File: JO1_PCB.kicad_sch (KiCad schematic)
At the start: 6 parts, among them J1 CN7, J2 CN8, J3 CN9, J4 CN10, U2 module_mpu6050

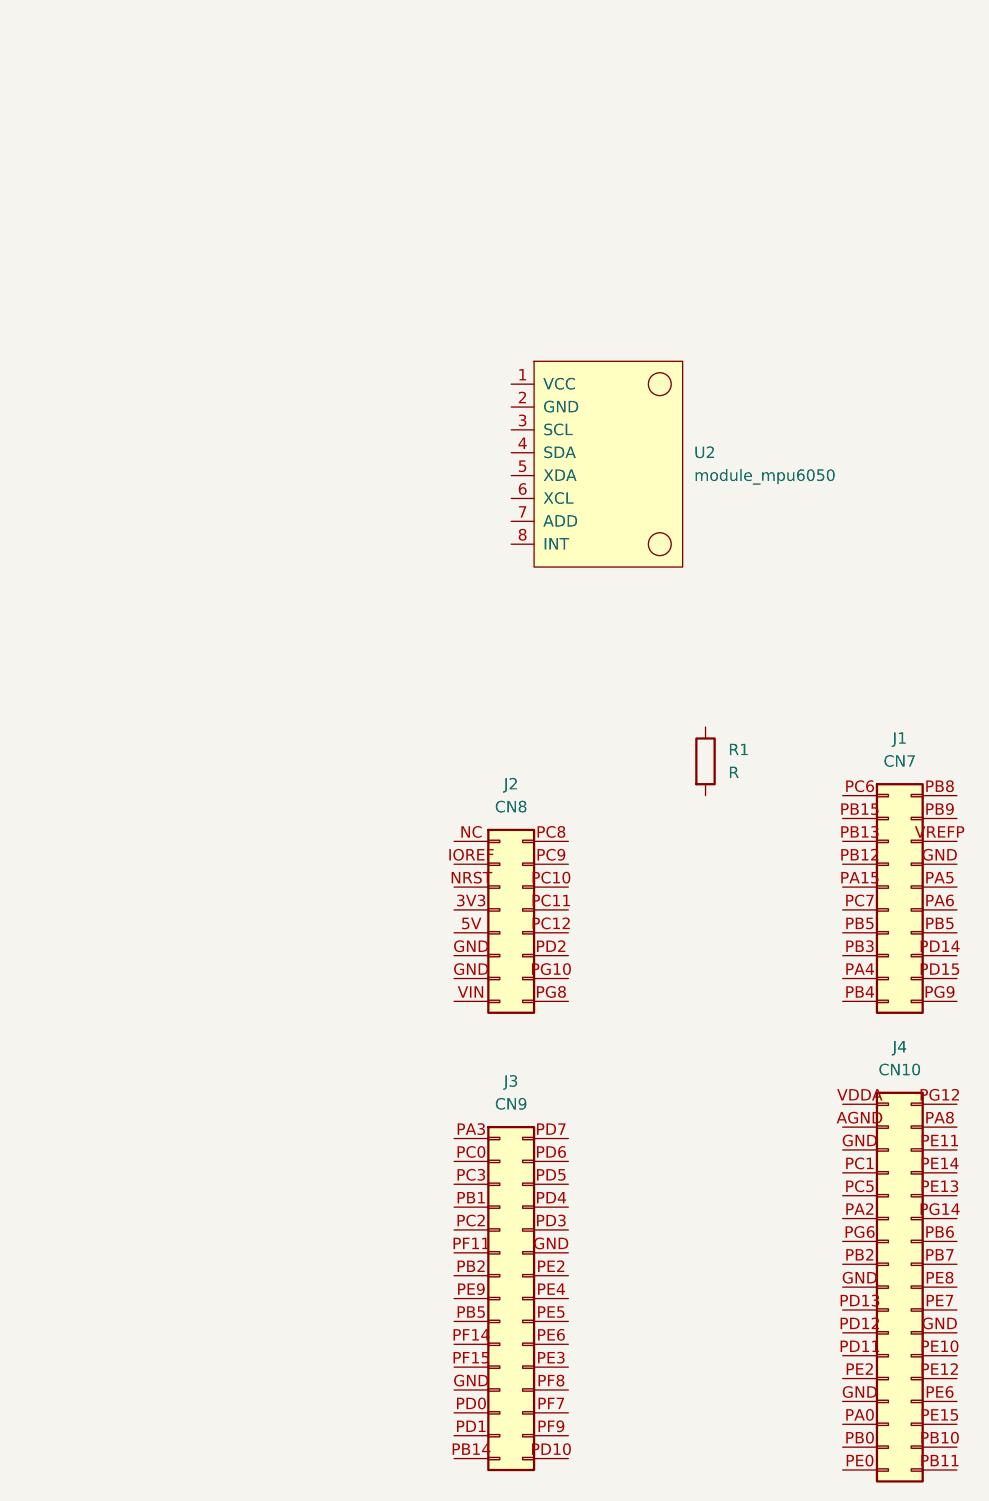
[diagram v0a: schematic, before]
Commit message: Corrected connectors
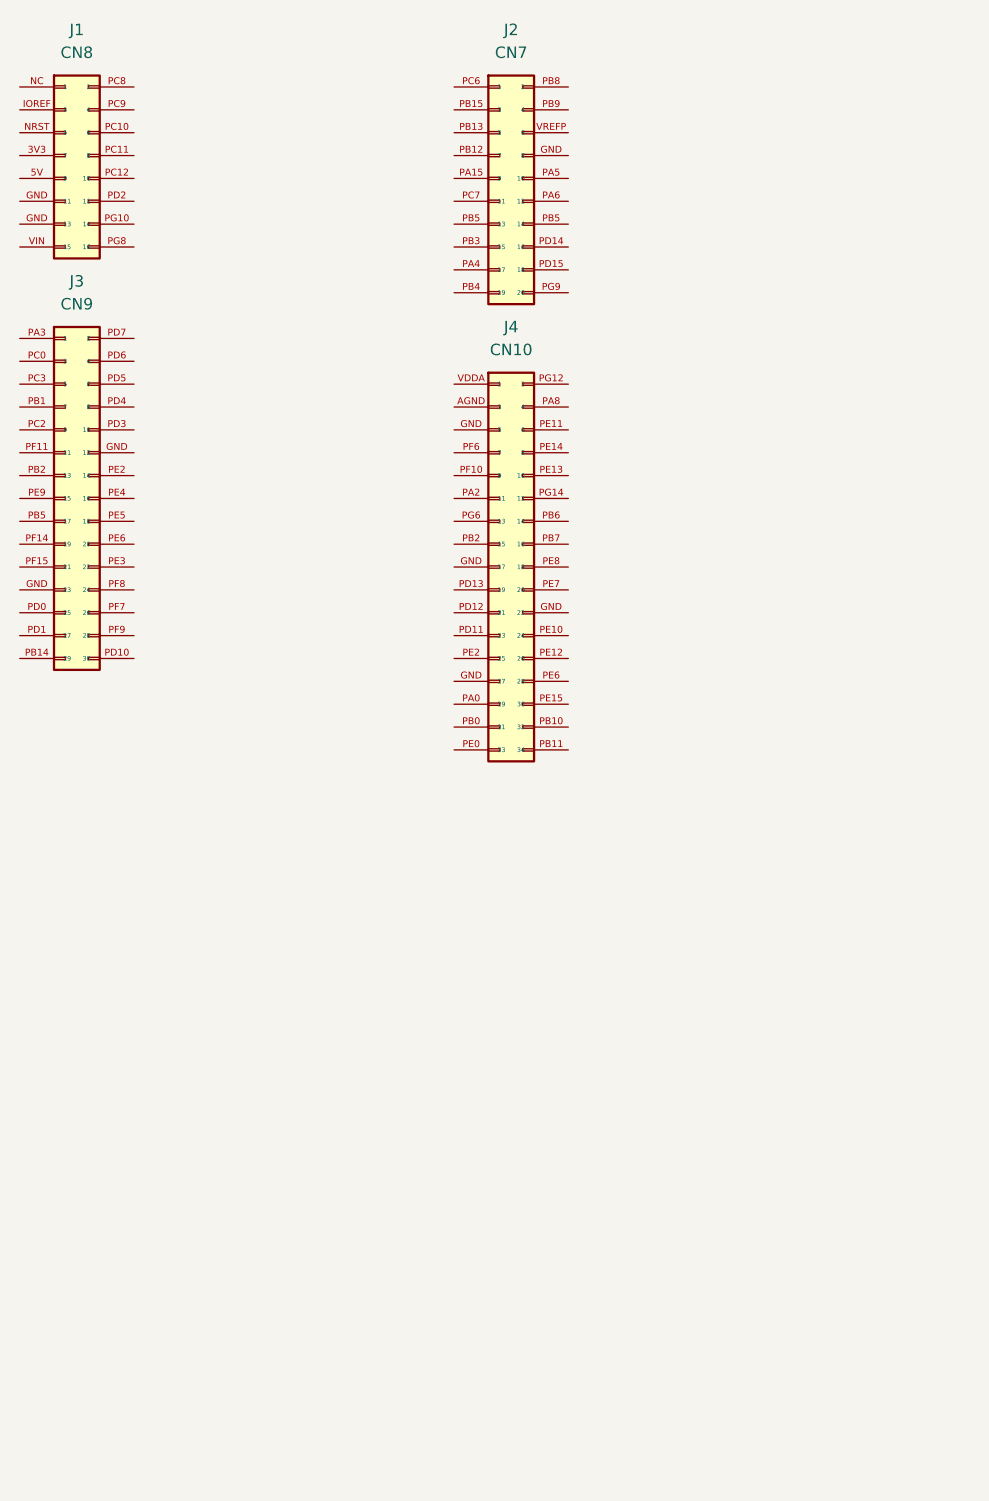
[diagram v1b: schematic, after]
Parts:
- removed R1: R, Resistor_THT:R_Axial_DIN0411_L9.9mm_D3.6mm_P15.24mm_Horizontal, symbol Device:R
- removed U2: module_mpu6050, usini_sensors:module_mpu6050, symbol USINI_SENSORS:module_mpu6050
- renumbered J2 to J1, J1 to J2

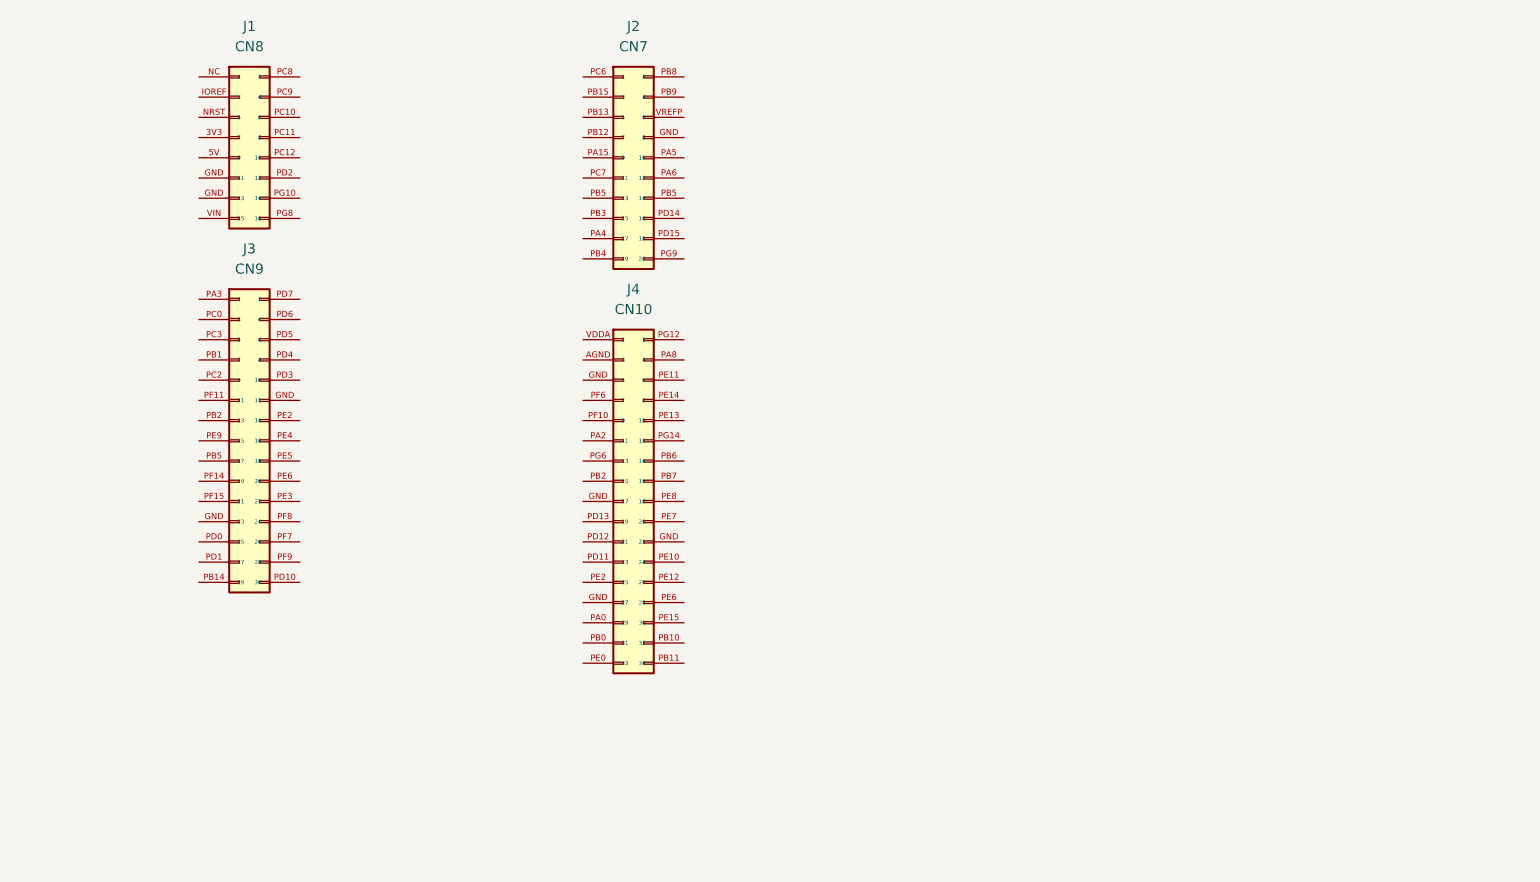
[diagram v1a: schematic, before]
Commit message: Added several components to the schematic
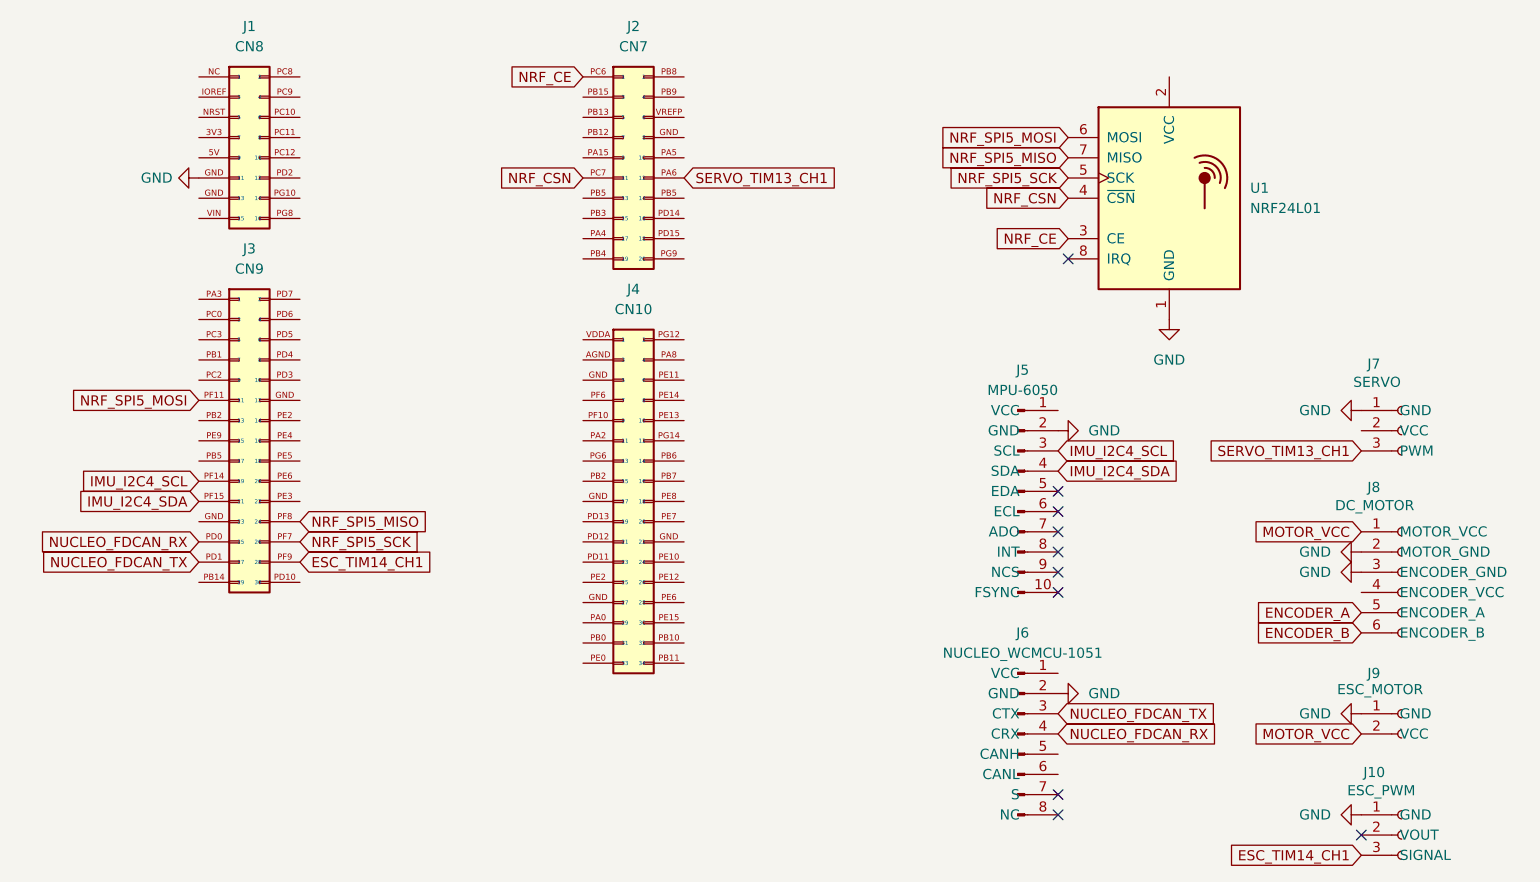
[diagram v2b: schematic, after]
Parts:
- added J10: ESC_PWM, Connector_PinHeader_2.54mm:PinHeader_1x03_P2.54mm_Vertical, symbol Connector:Conn_01x03_Socket
- added J5: MPU-6050, Connector_PinSocket_2.54mm:PinSocket_1x10_P2.54mm_Vertical, symbol Connector:Conn_01x10_Pin
- added J6: NUCLEO_WCMCU-1051, Connector_PinSocket_2.54mm:PinSocket_1x08_P2.54mm_Vertical, symbol Connector:Conn_01x08_Pin
- added J7: SERVO, Connector_PinHeader_2.54mm:PinHeader_1x03_P2.54mm_Vertical, symbol Connector:Conn_01x03_Socket
- added J8: DC_MOTOR, Connector_PinHeader_2.54mm:PinHeader_1x06_P2.54mm_Vertical, symbol Connector:Conn_01x06_Socket
- added J9: ESC_MOTOR, Connector_PinHeader_2.54mm:PinHeader_1x02_P2.54mm_Vertical, symbol Connector:Conn_01x02_Socket
- added U1: NRF24L01, RF_Module:nRF24L01_Breakout, symbol RF:NRF24L01_Breakout
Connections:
- net GND: now reaches J1.GND (13)
- net GND: now also J10.1 (GND), J5.2 (GND), J6.2 (GND), J7.1 (GND), J8.2 (MOTOR_GND), J8.3 (ENCODER_GND), J9.1 (GND), U1.1 (GND)
- net NUCLEO_FDCAN_RX: now reaches J3.PD0 (25)
- net NUCLEO_FDCAN_RX: now also J6.4 (CRX)
- net NUCLEO_FDCAN_TX: now reaches J3.PD1 (27)
- net NUCLEO_FDCAN_TX: now also J6.3 (CTX)
- net NRF_SPI5_MOSI: now reaches J3.PF11 (11)
- net NRF_SPI5_MOSI: now also U1.6 (MOSI)
- net IMU_I2C4_SCL: now reaches J3.PF14 (19)
- net IMU_I2C4_SCL: now also J5.3 (SCL)
- net IMU_I2C4_SDA: now reaches J3.PF15 (21)
- net IMU_I2C4_SDA: now also J5.4 (SDA)
- net NRF_SPI5_SCK: now reaches J3.PF7 (26)
- net NRF_SPI5_SCK: now also U1.5 (SCK)
- net NRF_SPI5_MISO: now reaches J3.PF8 (24)
- net NRF_SPI5_MISO: now also U1.7 (MISO)
- net ESC_TIM14_CH1: now reaches J3.PF9 (28)
- net ESC_TIM14_CH1: now also J10.3 (SIGNAL)
- net SERVO_TIM13_CH1: now reaches J2.PA6 (12)
- net SERVO_TIM13_CH1: now also J7.3 (PWM)
- net NRF_CE: now reaches J2.PC6 (1)
- net NRF_CE: now also U1.3 (CE)
- net NRF_CSN: now reaches J2.PC7 (11)
- net NRF_CSN: now also U1.4 (~{CSN})
- new net ENCODER_A: J8.5 (ENCODER_A)
- new net ENCODER_B: J8.6 (ENCODER_B)
- new net MOTOR_VCC: J8.1 (MOTOR_VCC), J9.2 (VCC)
- no-connect marks 0 -> 10

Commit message: avances.........
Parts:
- added J11: CAN_WCMCU-1051, Connector_PinSocket_2.54mm:PinSocket_1x08_P2.54mm_Vertical, symbol Connector:Conn_01x08_Pin
- added U2: BP, footprints:blue_pill, symbol bp:BP
- J6: value NUCLEO_WCMCU-1051 -> CAN_WCMCU-1051
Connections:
- net GND: now also J11.2 (GND)
- no-connect marks 10 -> 12

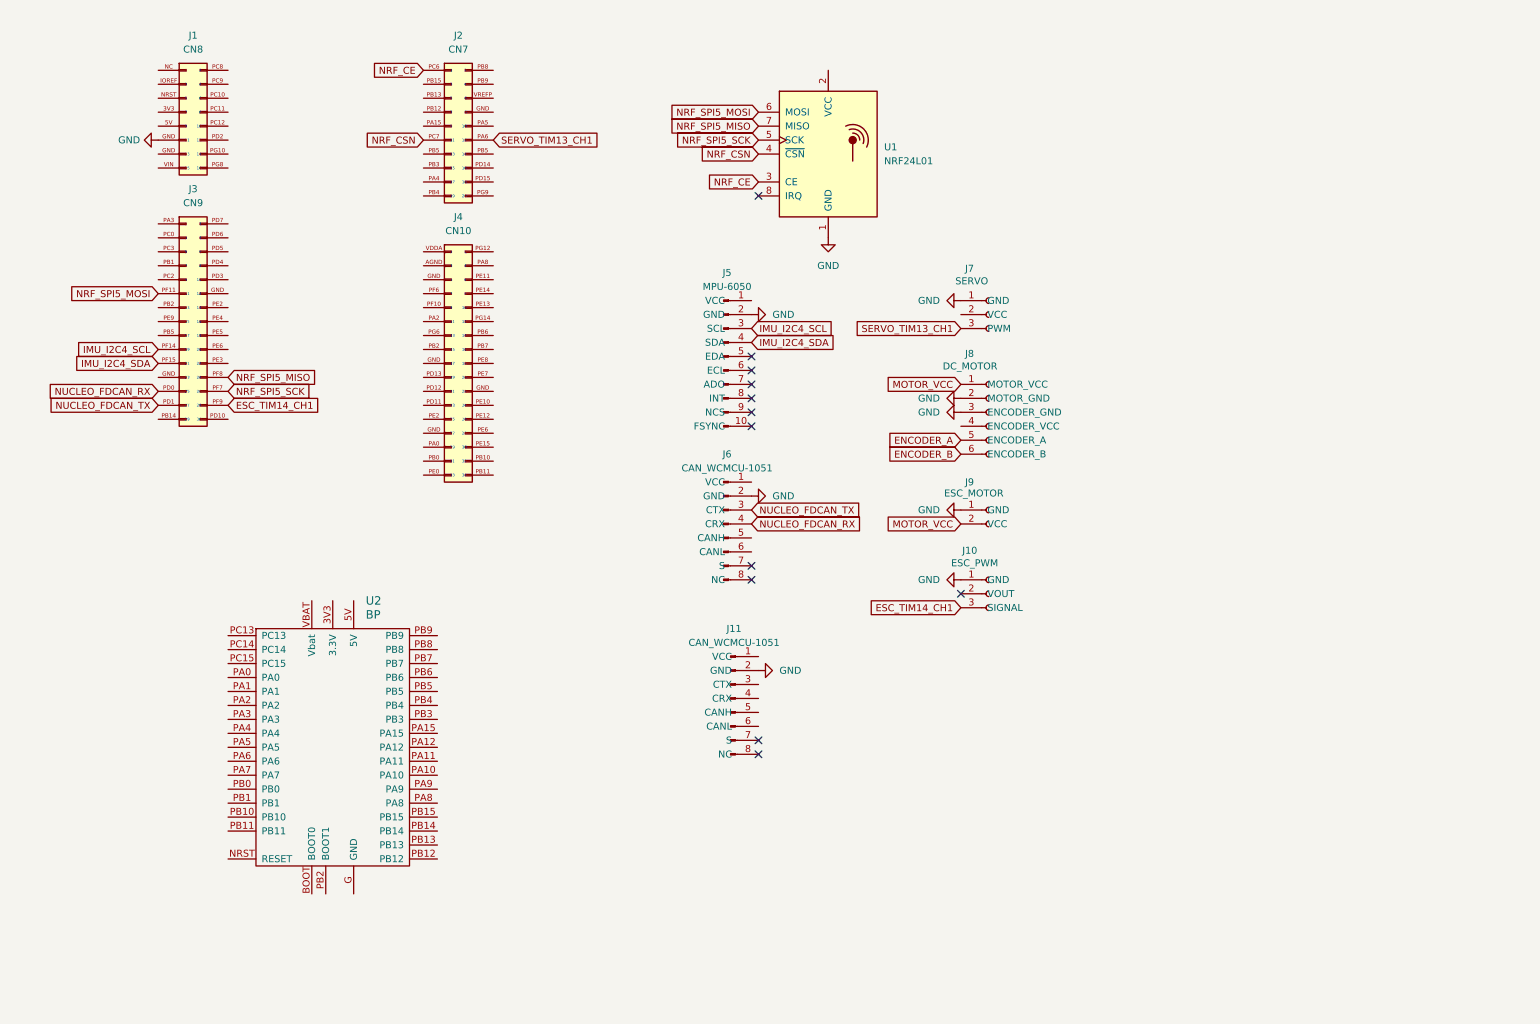
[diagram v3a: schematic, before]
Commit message: Modified global label
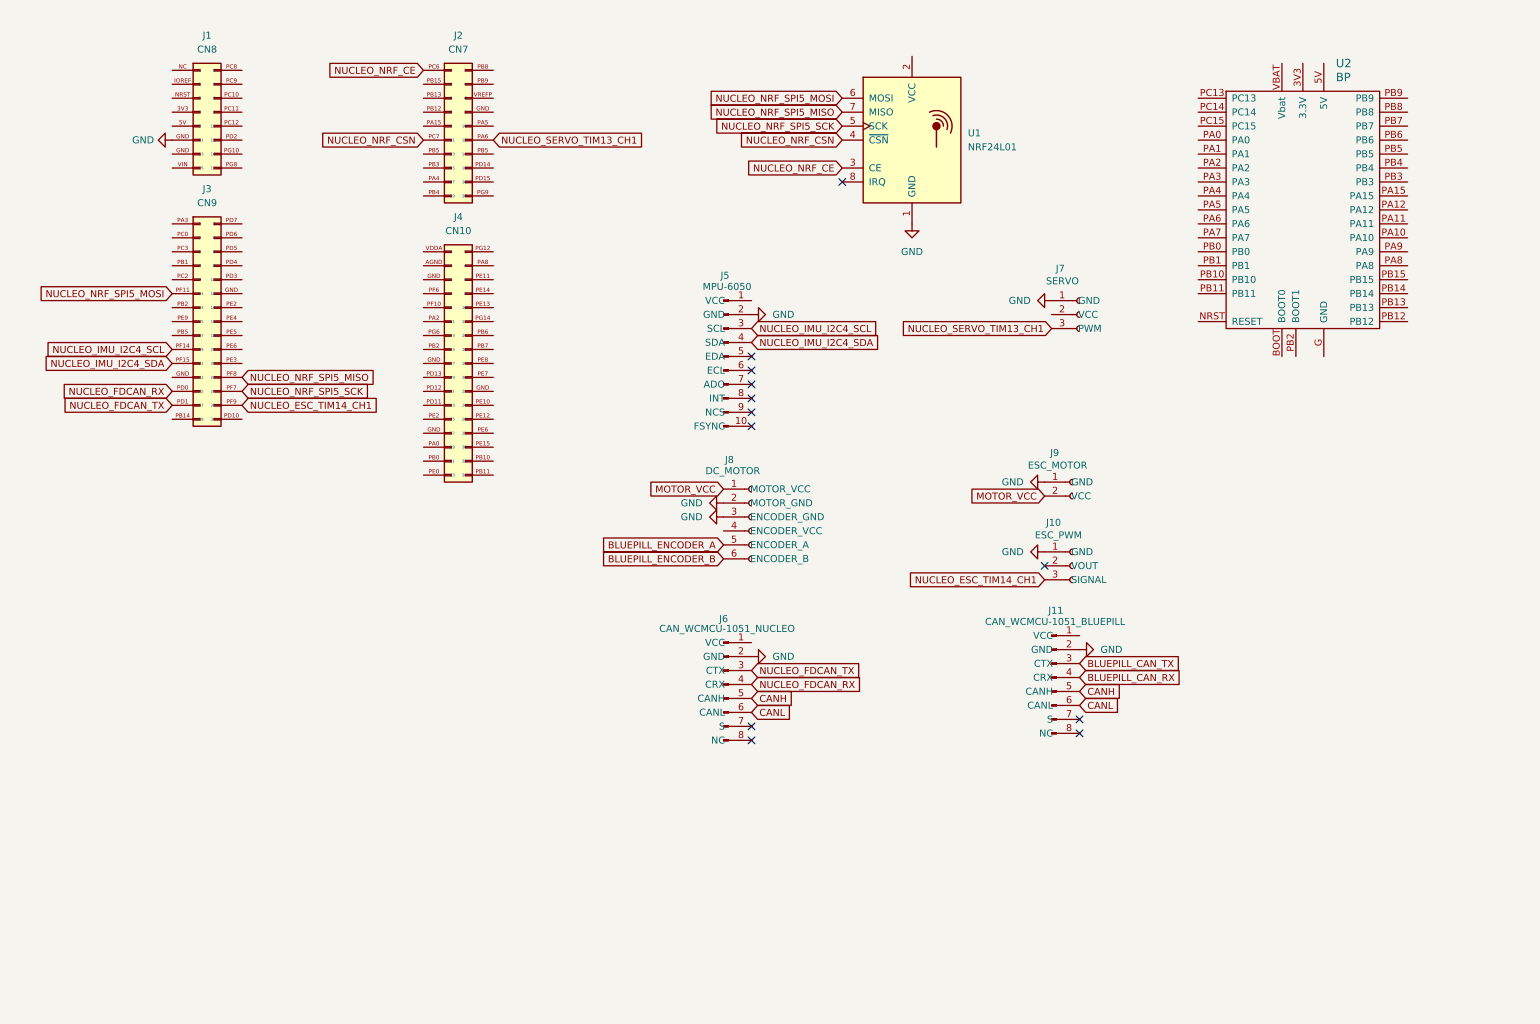
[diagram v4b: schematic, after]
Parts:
- J11: value CAN_WCMCU-1051 -> CAN_WCMCU-1051_BLUEPILL
- J6: value CAN_WCMCU-1051 -> CAN_WCMCU-1051_NUCLEO
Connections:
- net CANH: now reaches J6.5 (CANH)
- net CANH: now also J11.5 (CANH)
- net CANL: now reaches J6.6 (CANL)
- net CANL: now also J11.6 (CANL)
- net BLUEPILL_CAN_TX: now reaches J11.3 (CTX)
- net BLUEPILL_CAN_RX: now reaches J11.4 (CRX)
- net ENCODER_A renamed BLUEPILL_ENCODER_A
- net ENCODER_B renamed BLUEPILL_ENCODER_B
- net ESC_TIM14_CH1 renamed NUCLEO_ESC_TIM14_CH1
- net IMU_I2C4_SCL renamed NUCLEO_IMU_I2C4_SCL
- net IMU_I2C4_SDA renamed NUCLEO_IMU_I2C4_SDA
- net NRF_CE renamed NUCLEO_NRF_CE
- net NRF_CSN renamed NUCLEO_NRF_CSN
- net NRF_SPI5_MISO renamed NUCLEO_NRF_SPI5_MISO
- net NRF_SPI5_MOSI renamed NUCLEO_NRF_SPI5_MOSI
- net NRF_SPI5_SCK renamed NUCLEO_NRF_SPI5_SCK
- net SERVO_TIM13_CH1 renamed NUCLEO_SERVO_TIM13_CH1
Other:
- moved on the sheet: J1, J10, J11, J3, J6, J7, J8, J9, U1, U2
